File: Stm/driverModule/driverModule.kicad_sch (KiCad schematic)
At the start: 23 parts, among them J101 Conn_02x13_Odd_Even, J102 AXK520147YG, J103 Conn_02x08_Odd_Even, J104 AXK520147YG, U101 74HC165, U102 ADM7171ACPZ-3.0-R7, U103 TJA1051T-3, U104 TPS5410DR, U107 74HC165

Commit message: Remove Connector
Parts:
- removed J102, J104: AXK520147YG, Local_Footprints:AXK520147YG, symbol _Connectors:AXK520147YG
- added J102: DF40HC3.5-30DS-0.4V51, CONN_DF40HC3.5-30DS-0.4V51_HIR, symbol con-hirose-df40:DF40HC3.5-30DS-0.4V51
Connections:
- net GND: now also J102.1
- net MirrorMotorsEnable: now also J102.11
- net MirrorSpiChipSelect: now also J102.17
- net SpiClock: now also J102.5
- net SpiMasterInput: now also J102.7
- net SpiMasterOutput: now also J102.9
- no-connect marks 31 -> 24

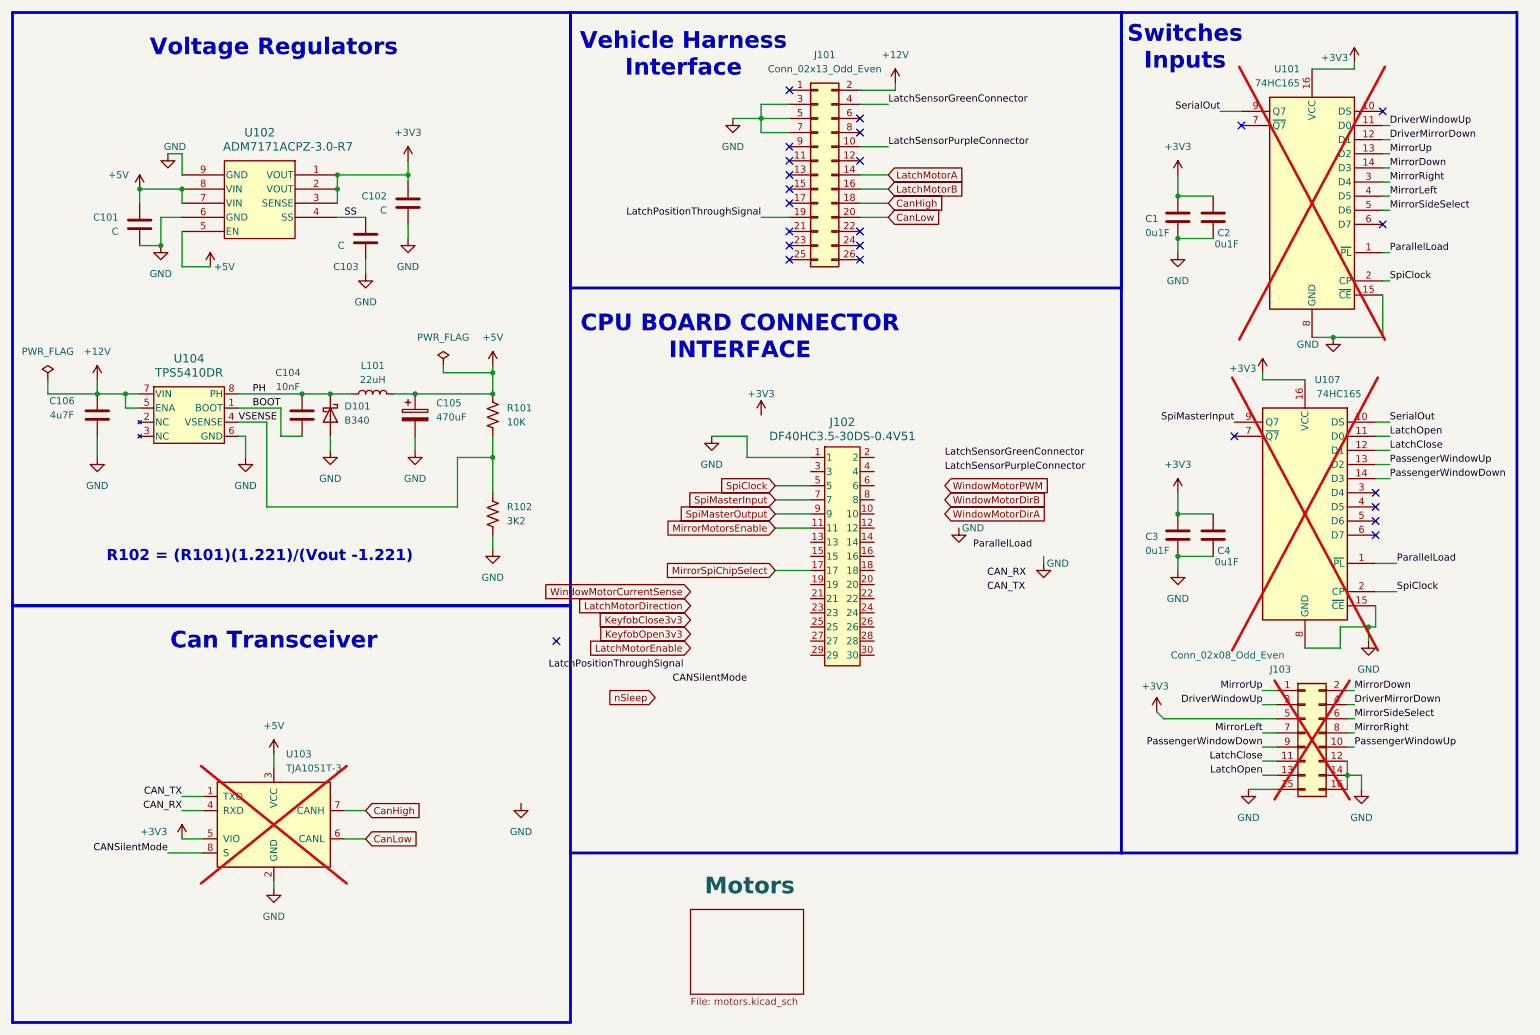
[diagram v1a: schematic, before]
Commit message: Changed Connector
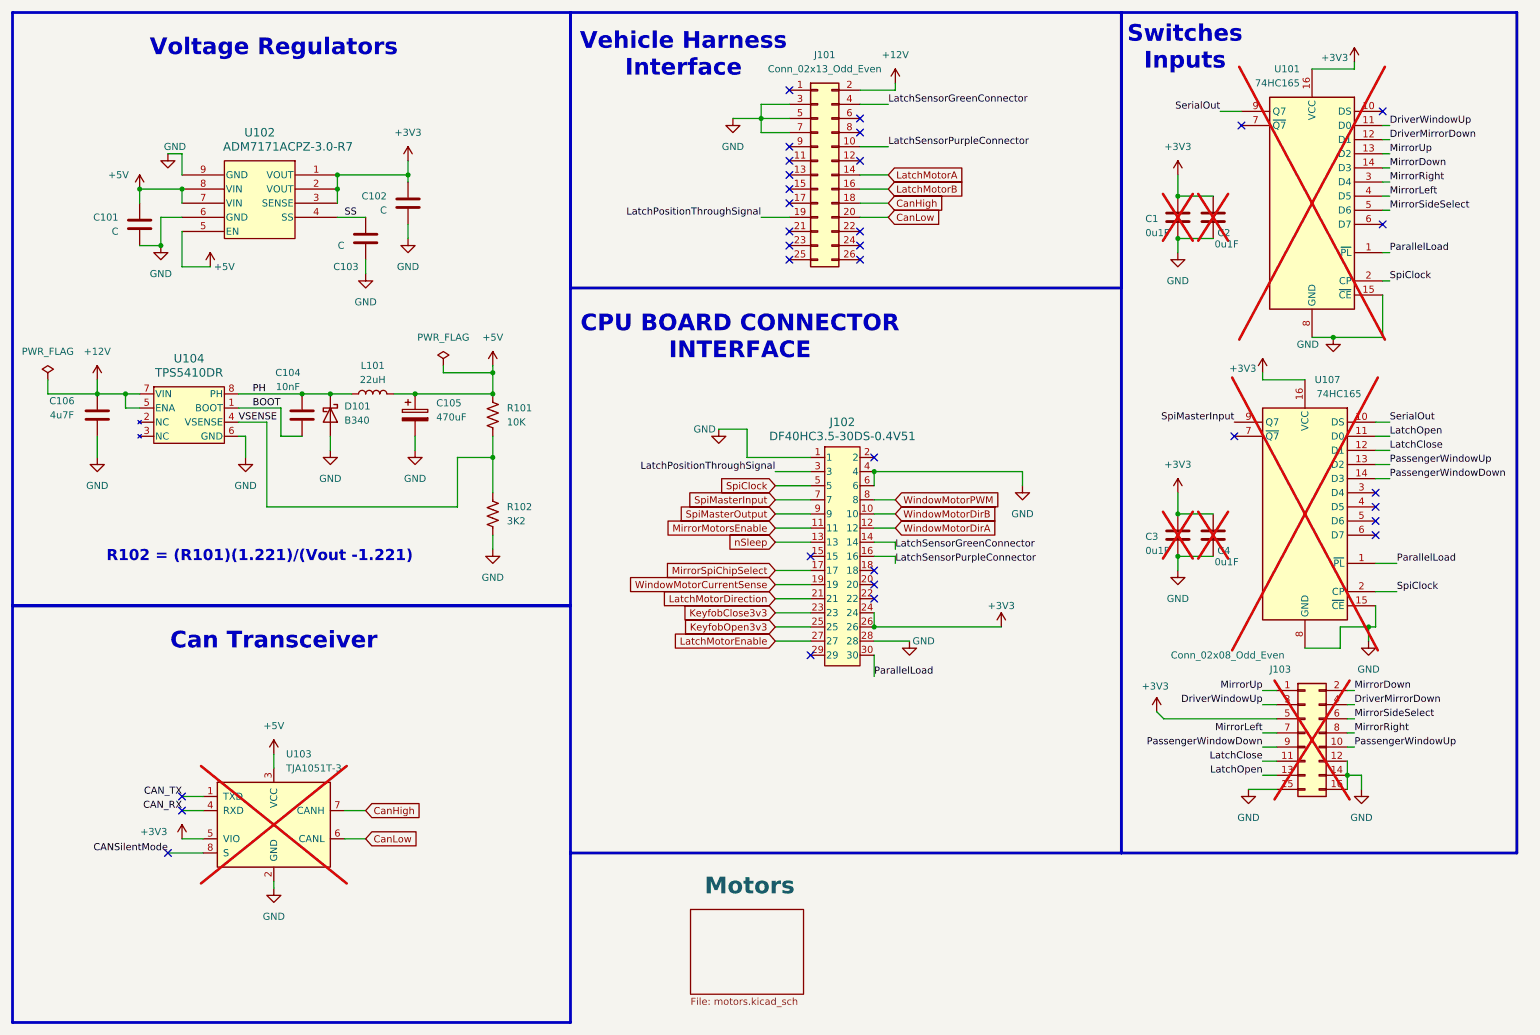
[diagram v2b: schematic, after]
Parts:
- C1, C2, C3, C4: now not fitted
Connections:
- net +3V3: now also J102.24, J102.26
- net GND: now also J102.28, J102.4, J102.6
- net KeyfobClose3v3: now also J102.23
- net KeyfobOpen3v3: now also J102.25
- net LatchMotorDirection: now also J102.21
- net LatchMotorEnable: now also J102.27
- net LatchPositionThroughSignal: now also J102.3
- net LatchSensorGreenConnector: now also J102.14
- net LatchSensorPurpleConnector: now also J102.16
- net ParallelLoad: now also J102.30
- net WindowMotorCurrentSense: now also J102.19
- net WindowMotorDirA: now also J102.12
- net WindowMotorDirB: now also J102.10
- net WindowMotorPWM: now also J102.8
- net nSleep: now also J102.13
- no-connect marks 24 -> 32

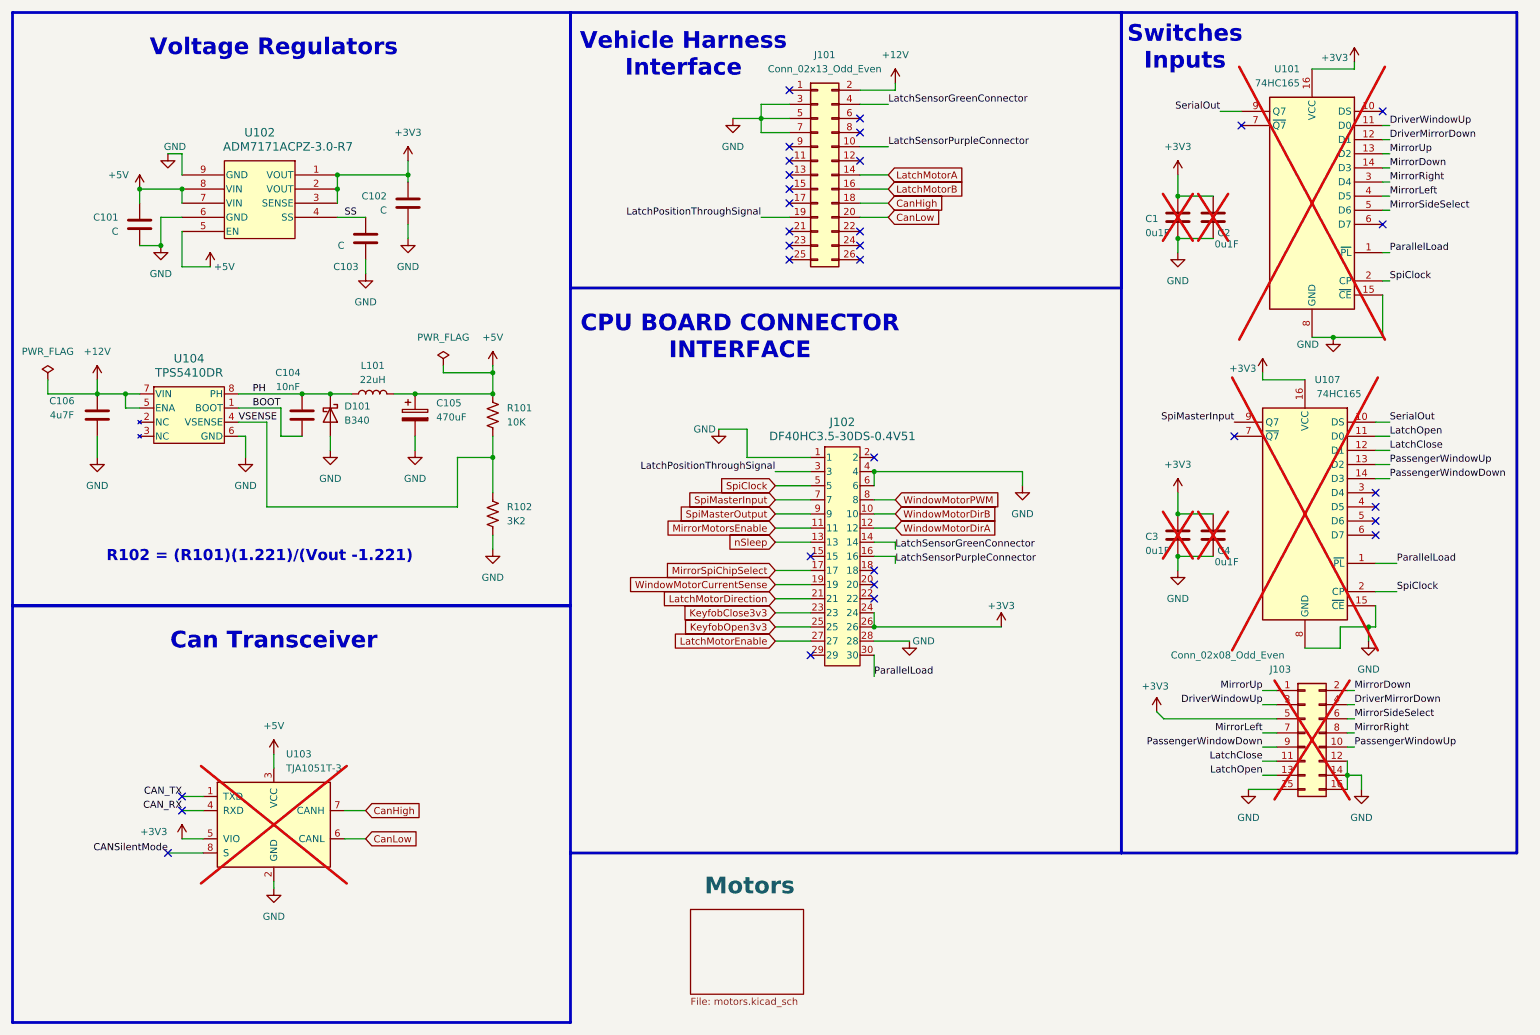
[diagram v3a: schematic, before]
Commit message: Driver Board
Modify driver module for the PCI express cpu card
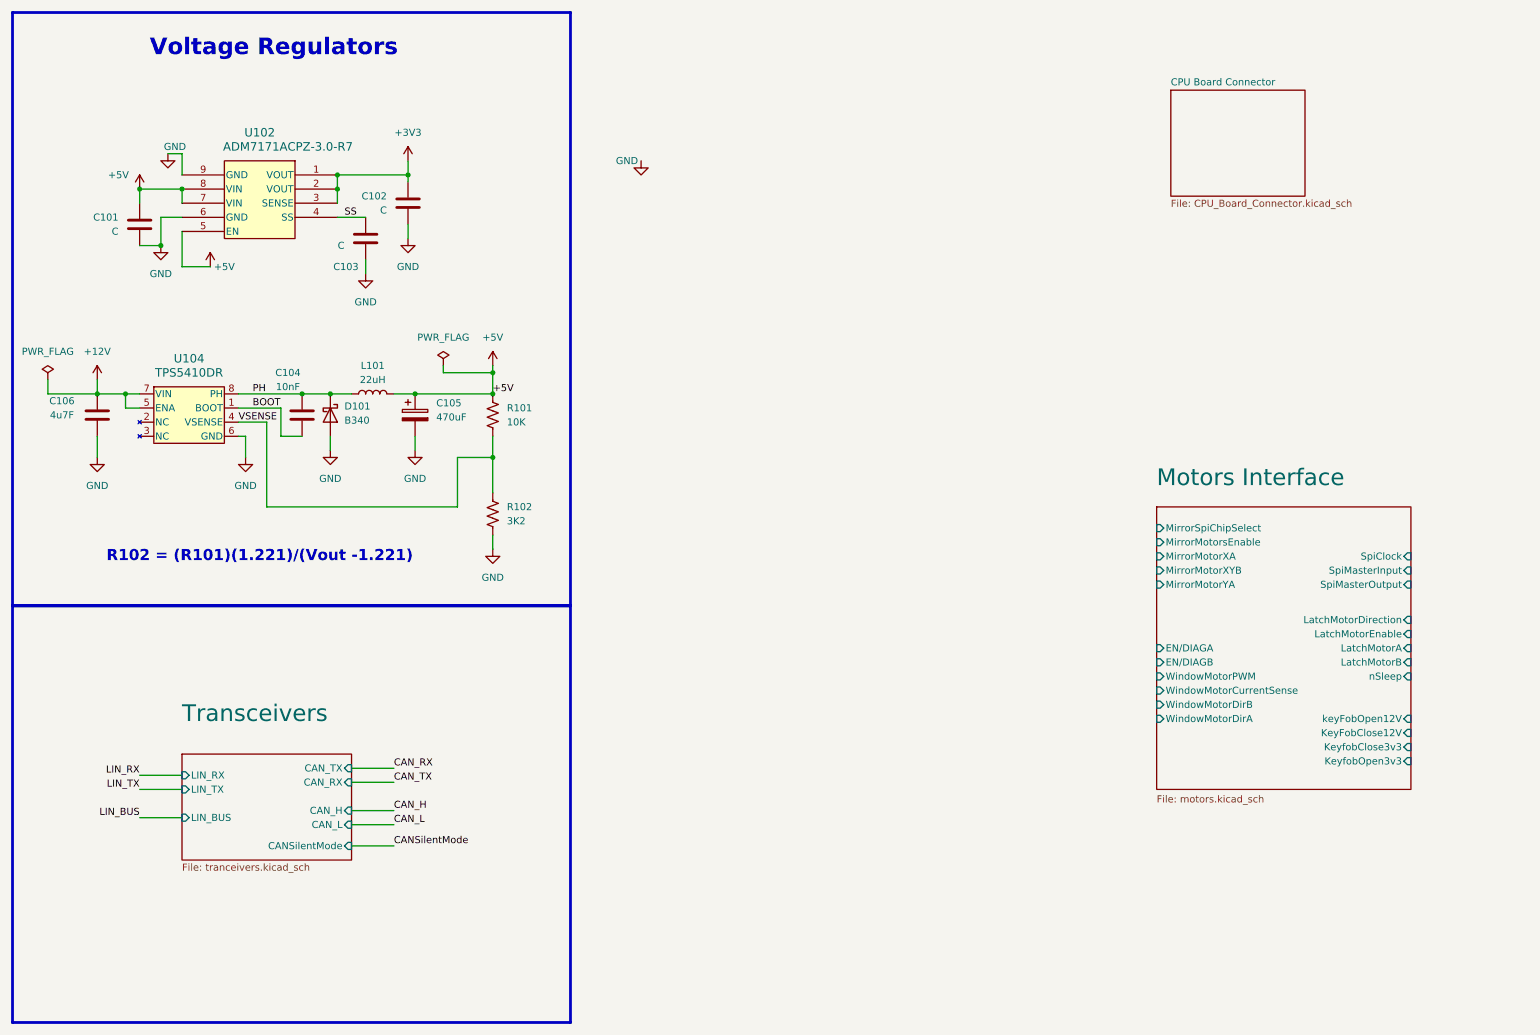
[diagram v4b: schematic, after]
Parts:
- removed C1, C2, C3, C4: 0u1F, Capacitor_SMD:C_0402_1005Metric_Pad0.74x0.62mm_HandSolder, symbol Device:C
- removed J101: Conn_02x13_Odd_Even, Connector_PinHeader_2.54mm:PinHeader_2x13_P2.54mm_Vertical, symbol Connector_Generic:Conn_02x13_Odd_Even
- removed J102: DF40HC3.5-30DS-0.4V51, CONN_DF40HC3.5-30DS-0.4V51_HIR, symbol con-hirose-df40:DF40HC3.5-30DS-0.4V51
- removed J103: Conn_02x08_Odd_Even, Connector_PinHeader_2.54mm:PinHeader_2x08_P2.54mm_Vertical, symbol Connector_Generic:Conn_02x08_Odd_Even
- removed U101, U107: 74HC165, Package_SO:TSSOP-16_4.4x5mm_P0.65mm, symbol 74xx:74HC165
- removed U103: TJA1051T-3, Package_SO:SOIC-8_3.9x4.9mm_P1.27mm, symbol Interface_CAN_LIN:TJA1051T-3
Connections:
- no-connect marks 32 -> 0
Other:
- sheet Motors renamed Motors Interface
- added sheet CPU Board Connector (CPU_Board_Connector.kicad_sch)
- added sheet Transceivers (tranceivers.kicad_sch)
- sheet Motors Interface ports: added EN/DIAGA, EN/DIAGB, KeyFobClose12V, KeyfobClose3v3, KeyfobOpen3v3, LatchMotorA, LatchMotorB, LatchMotorDirection, LatchMotorEnable, MirrorMotorXA, MirrorMotorXYB, MirrorMotorYA, MirrorMotorsEnable, MirrorSpiChipSelect, SpiClock, SpiMasterInput, SpiMasterOutput, WindowMotorCurrentSense, WindowMotorDirA, WindowMotorDirB, WindowMotorPWM, keyFobOpen12V, nSleep; removed none
- note removed: "CPU BOARD CONNECTOR INTERFACE"
- note removed: "Can Transceiver"
- note removed: "Switches Inputs"
- note removed: "Vehicle Harness Interface"
